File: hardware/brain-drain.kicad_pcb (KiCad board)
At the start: 4 copper layers, 150 x 112 mm, 302 parts, among them J10 SATA 22-pin, J11 SATA 22-pin, J12 SATA 22-pin, J13 SATA 22-pin, J21 KPJX-4S-S, J3 microSD, J40 Fan GND/5V/TACH/PWM, J41 OLED GND/VCC/SCL/SDA, J5 USB-C rpiboot, J50 M.2 M-key, J6 nRPIBOOT, J7 UART0 GND/TX/RX, M1 CM5002016, Q20 AO4407A, Q31 P-FET -30V 6A DFN3x3, Q32 P-FET -30V 6A DFN3x3, Q33 P-FET -30V 6A DFN3x3, Q34 P-FET -30V 6A DFN3x3, Q41 P-FET -30V 6A DFN3x3, Q42 P-FET -30V 6A DFN3x3, Q43 P-FET -30V 6A DFN3x3, Q44 P-FET -30V 6A DFN3x3, Q51 2N7002, Q52 2N7002, Q53 2N7002, Q54 2N7002, Q61 2N7002, Q62 2N7002, Q63 2N7002, Q64 2N7002, SW1 DIP x8, SW3 lid microswitch, U1 USB5744/2G, U10 ASM1153E, U11 ASM1153E, U12 ASM1153E, U13 ASM1153E, U2 USB5744/2G, U20 TPS56637RPAR, U21 TPS56637RPAR, U22 AP63203WU-7, U3 AP2112K-1.2, U50 TPS22965DSGR, U51 AP63203WU-7, U52 TPS22965DSGR, Y1 25MHz CL=20pF, Y10 30MHz CL=16pF, Y11 30MHz CL=16pF, Y12 30MHz CL=16pF, Y13 30MHz CL=16pF, Y2 25MHz CL=20pF

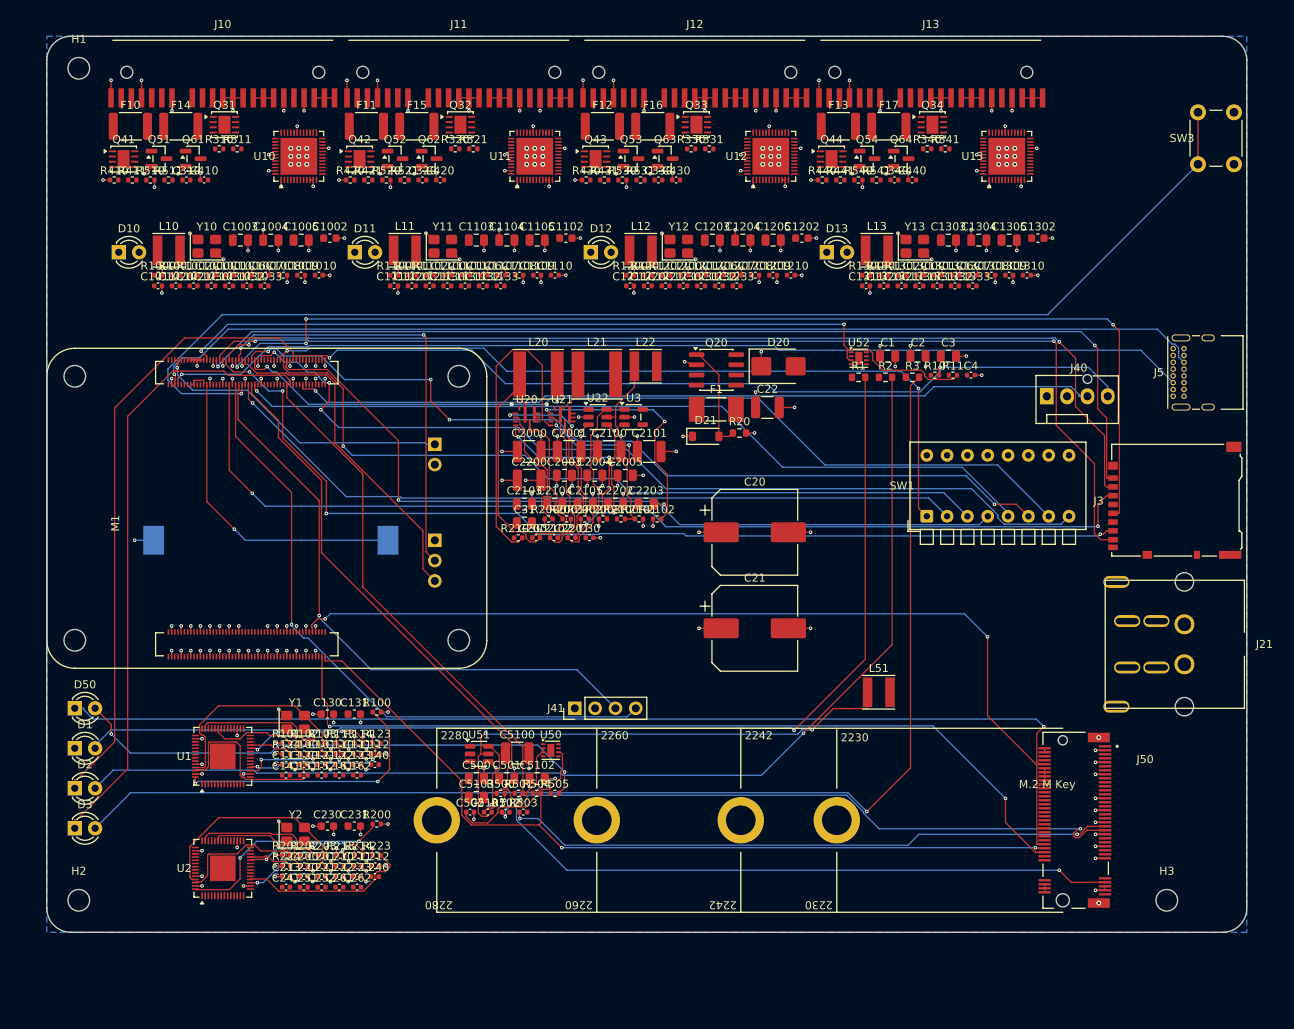
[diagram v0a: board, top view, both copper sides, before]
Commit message: hw(v3): staged autoroute on the 150x112 board — 83 % of connections, 21 of 48 pairs, DRC copper-clean
- stage 2 rerun after stripping the QFN via rings (the connector fanout now skips QFNs), stage 3 on
  freerouting 2.4.1, drc-clean, final fanouts: 3300 segments, 738 vias, 151 connections open
- docs: STATUS board row / R4 / R22, D7 outcome and D8 (0.3/0.15 mm vias for the QFN supply pins),
  CHANGELOG, tracker, README, FABRICATION gate 1; board renders

Co-Authored-By: Claude Fable 5.1 <noreply@anthropic.com>
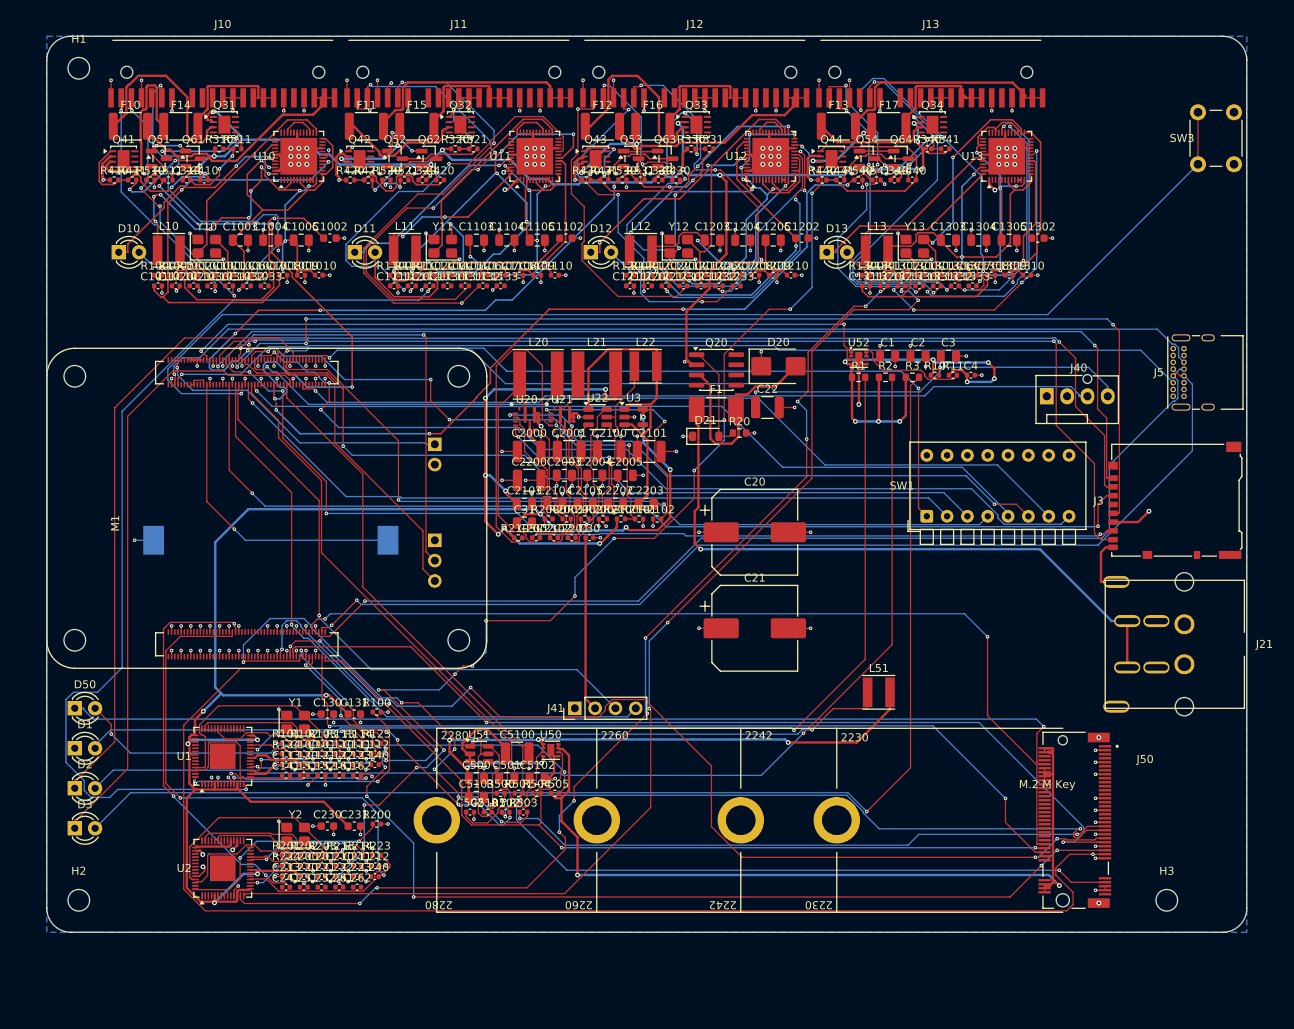
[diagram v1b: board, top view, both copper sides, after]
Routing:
- net +1V2: track 0.00 -> 213.0 mm, vias 0 -> 10
- net +12V: track 24.1 -> 198.6 mm, vias 14 -> 28
- net PCIE_CLK_P: track 0.00 -> 165.5 mm, vias 0 -> 1
- net BAY3_USB3_RX_N: track 0.00 -> 143.1 mm, vias 0 -> 16
- net BAY4_USB3_TX_N: track 0.00 -> 140.4 mm, vias 0 -> 4
- net BAY4_USB3_TX_P: track 0.00 -> 133.9 mm, vias 0 -> 10
- net USB2_DM: track 0.00 -> 130.5 mm, vias 0 -> 2
- net USB2_DP: track 0.00 -> 129.8 mm, vias 0 -> 1
- net PCIE_CLK_N: track 0.00 -> 128.3 mm, vias 0 -> 8
- net PCIE_TX_N: track 0.00 -> 124.1 mm, vias 0 -> 5
- net BAY2_USB3_TX_N: track 0.00 -> 120.3 mm, vias 0 -> 2
- net +3V3: track 24.9 -> 143.3 mm, vias 28 -> 30
- net PCIE_TX_P: track 0.00 -> 118.3 mm, vias 0 -> 2
- net 3V3_M2_SW: track 3.50 -> 106.5 mm, vias 0 -> 2
- net BAY_EN4: track 0.00 -> 95.6 mm, vias 0 -> 4
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
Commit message: hw(routing): D8 applied — 0.3/0.15 mm dog-bone vias on the QFN pins (fanout_qfn), unattended routing chain; D9 brief on bay cards / 8 ports
- route.py: fanout_qfn (two staggered via lines, all multi-pin non-pair nets), min via 0.3/0.15 and hole
  clearance 0.2 in the project rules; tools/route_chain.sh runs stage 2, stage 3, cleanup, fanouts,
  reports and renders unattended
- fresh v3 board with all four fanouts: 441 vias before routing, DRC clean; stage 1 routed in 2 minutes
- docs: decisions/2026-09-23-bay-cards.md (D9), DECISIONS D8/D9

Co-Authored-By: Claude Fable 5.1 <noreply@anthropic.com>
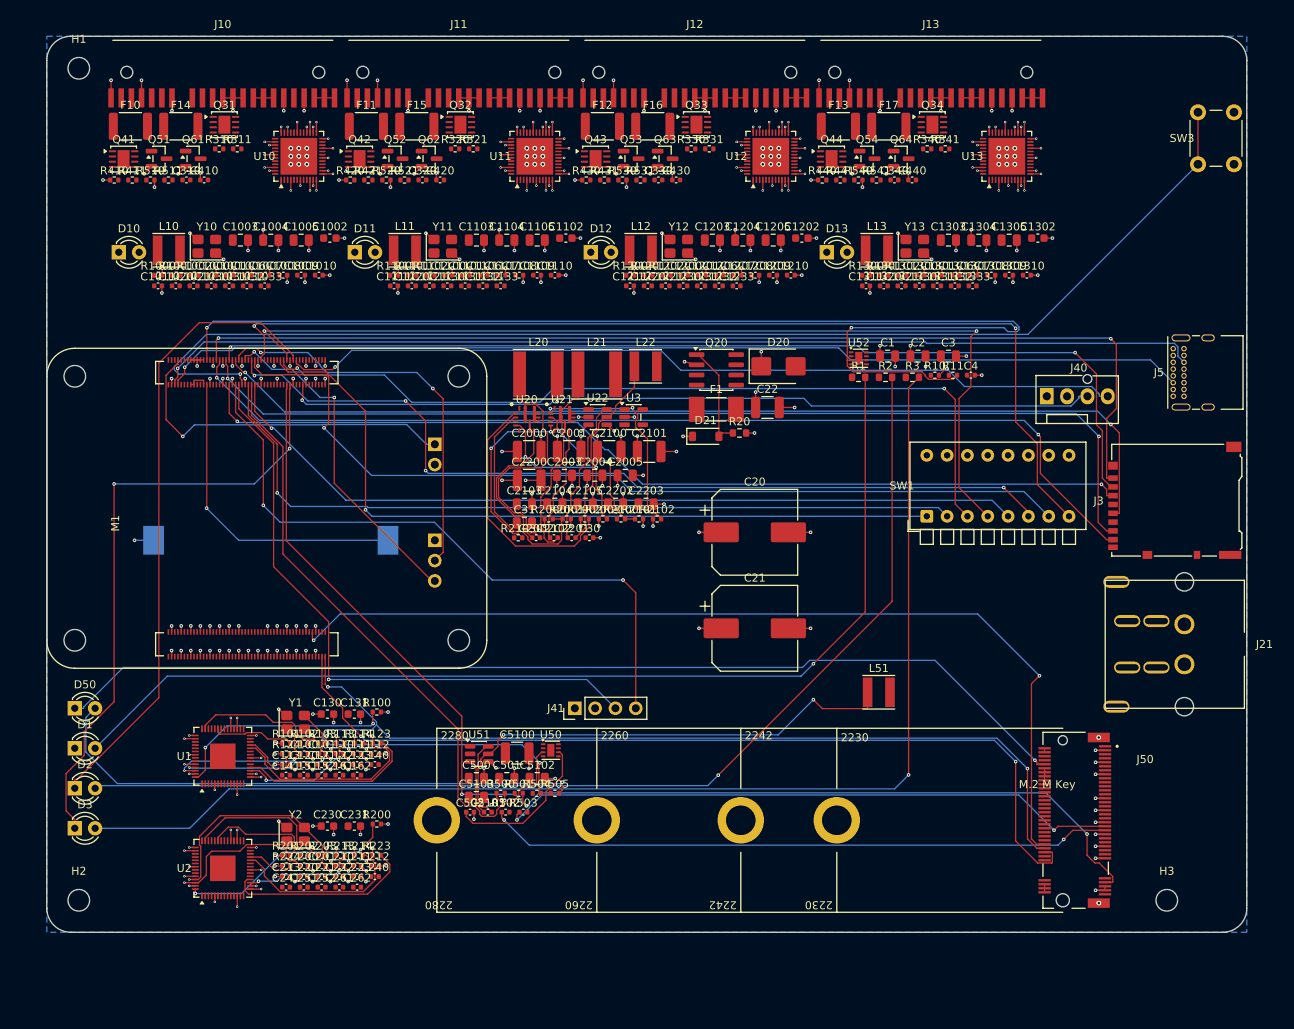
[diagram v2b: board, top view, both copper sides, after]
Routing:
- net +1V2: track 213.0 -> 17.0 mm, vias 10 -> 16
- net +12V: track 198.6 -> 24.1 mm, vias 28 -> 14
- net PCIE_CLK_P: track 165.5 -> 0.00 mm, vias 1 -> 0
- net BAY3_USB3_RX_N: track 143.1 -> 0.00 mm, vias 16 -> 0
- net BAY4_USB3_TX_N: track 140.4 -> 0.00 mm, vias 4 -> 0
- net BAY4_USB3_TX_P: track 133.9 -> 0.00 mm, vias 10 -> 0
- net USB2_DM: track 130.5 -> 0.00 mm, vias 2 -> 0
- net USB2_DP: track 129.8 -> 0.00 mm, vias 1 -> 0
- net PCIE_CLK_N: track 128.3 -> 0.00 mm, vias 8 -> 0
- net PCIE_TX_N: track 124.1 -> 0.00 mm, vias 5 -> 0
- net BAY2_USB3_TX_N: track 120.3 -> 0.00 mm, vias 2 -> 0
- net PCIE_TX_P: track 118.3 -> 0.00 mm, vias 2 -> 0
- net +3V3: track 143.3 -> 26.6 mm, vias 30 -> 28
- net 3V3_M2_SW: track 106.5 -> 3.50 mm, vias 2 -> 0
- net BAY_EN4: track 95.6 -> 0.00 mm, vias 4 -> 0
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
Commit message: docs: C24 brain + bay cards — decisions, architecture, BOM card table, fabrication, README, USAGE, STATUS, changelog, history; diagrams: 8 slots, lid plan, left wall
Co-Authored-By: Claude Fable 5.1 <noreply@anthropic.com>
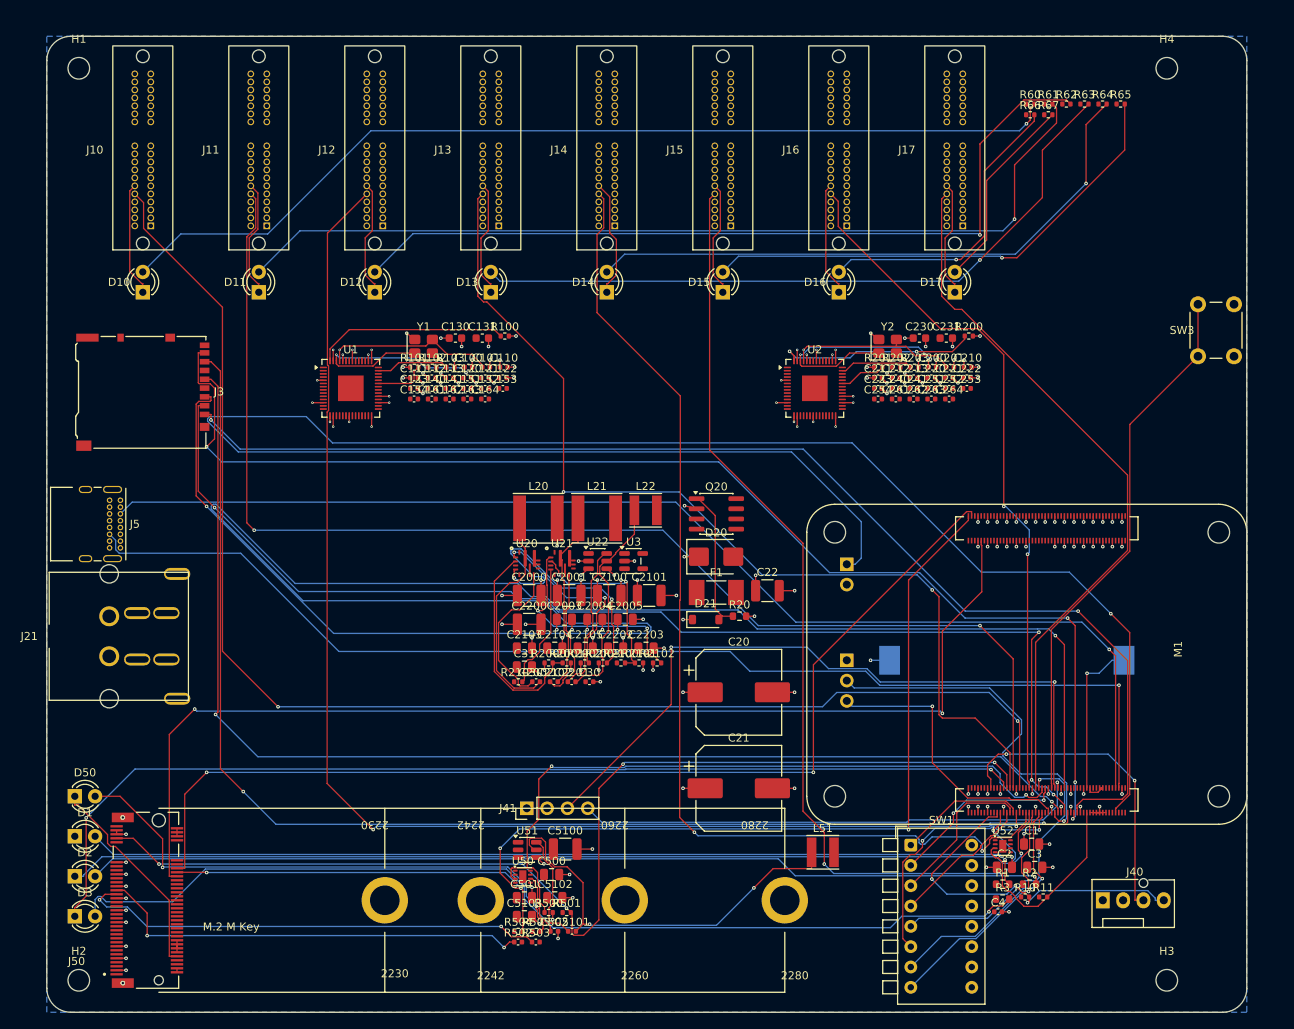
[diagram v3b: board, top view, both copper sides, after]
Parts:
- removed C1008, C1009, C1010, C1011, C1020, C1021, C1106, C1107, C1108, C1109, C1110, C1111, C1120, C1121, C1206, C1207, C1208, C1209, C1210, C1211, C1220, C1221, C1306, C1307, C1308, C1309, C1310, C1311, C1320, C1321, C310, C320, C330, C340, C410, C420, C430, C440: 100n, Capacitor_SMD:C_0402_1005Metric
- removed C1030, C1031, C1032, C1033, C1130, C1131, C1132, C1133, C1230, C1231, C1232, C1233, C1330, C1331, C1332, C1333: 10n, Capacitor_SMD:C_0402_1005Metric
- removed C1100, C1101, C1200, C1201, C1300, C1301: 22p, Capacitor_SMD:C_0402_1005Metric
- removed C1102, C1202, C1302: 2.2u, Capacitor_SMD:C_0603_1608Metric
- removed C1103, C1104, C1105, C1203, C1204, C1205, C1303, C1304, C1305: 10u 10V, Capacitor_SMD:C_0805_2012Metric
- removed F10, F11, F12, F13: 3A hold 1812, Fuse:Fuse_1812_4532Metric
- removed F14, F15, F16, F17: 2A hold 1812, Fuse:Fuse_1812_4532Metric
- removed L11, L12, L13: 4.7u 1A, Inductor_SMD:L_Taiyo-Yuden_NR-40xx
- removed Q31, Q32, Q33, Q34, Q41, Q42, Q43, Q44: P-FET -30V 6A DFN3x3, Package_DFN_QFN:DFN-8-1EP_3x3mm_P0.65mm_EP1.5x2.25mm
- removed Q51, Q52, Q53, Q54, Q61, Q62, Q63, Q64: 2N7002, Package_TO_SOT_SMD:SOT-23
- removed R1100, R1200, R1300: 12.1k 1%, Resistor_SMD:R_0402_1005Metric
- removed R1101, R1201, R1301, R311, R321, R331, R341, R411, R421, R431, R441, R510, R520, R530, R540: 10k, Resistor_SMD:R_0402_1005Metric
- removed R1102, R1202, R1302: 470, Resistor_SMD:R_0402_1005Metric
- removed R310, R320, R330, R340, R410, R420, R430, R440: 100k, Resistor_SMD:R_0402_1005Metric
- removed R511, R521, R531, R541: 1k, Resistor_SMD:R_0402_1005Metric
- removed Y11, Y12, Y13: 30MHz CL=16pF, Crystal:Crystal_SMD_3225-4Pin_3.2x2.5mm
- BT1: renamed from J6; value nRPIBOOT -> CR2032; footprint Connector_PinHeader_2.54mm:PinHeader_1x02_P2.54mm_Vertical -> Battery:BatteryHolder_Keystone_1060_1x2032
- C1: renamed from R3; value 1k -> 22u 10V; footprint Resistor_SMD:R_0603_1608Metric -> Capacitor_SMD:C_0805_2012Metric
- C101: renamed from C110; value 100n -> 33p
- C130: renamed from R103; value 200k -> 4.7u 10V; footprint Resistor_SMD:R_0402_1005Metric -> Capacitor_SMD:C_0603_1608Metric
- C131: renamed from R113; value 10k -> 4.7u 10V; footprint Resistor_SMD:R_0402_1005Metric -> Capacitor_SMD:C_0603_1608Metric
- C154: renamed from Y2; value 25MHz CL=20pF -> 100n; footprint Crystal:Crystal_SMD_3225-4Pin_3.2x2.5mm -> Capacitor_SMD:C_0402_1005Metric
- C161: renamed from C230; value 4.7u 10V -> 100n; footprint Capacitor_SMD:C_0603_1608Metric -> Capacitor_SMD:C_0402_1005Metric
- C162: renamed from C231; value 4.7u 10V -> 100n; footprint Capacitor_SMD:C_0603_1608Metric -> Capacitor_SMD:C_0402_1005Metric
- C163: renamed from R200; value 12.0k 1% -> 100n; footprint Resistor_SMD:R_0402_1005Metric -> Capacitor_SMD:C_0402_1005Metric
- C164: renamed from R201; value 10k -> 100n; footprint Resistor_SMD:R_0402_1005Metric -> Capacitor_SMD:C_0402_1005Metric
- C2: renamed from R10; value 10k -> 22u 10V; footprint Resistor_SMD:R_0402_1005Metric -> Capacitor_SMD:C_0805_2012Metric
- C2000: renamed from C2003; value 22u 10V -> 10u 25V; footprint Capacitor_SMD:C_0805_2012Metric -> Capacitor_SMD:C_1210_3225Metric
- C2001: renamed from C2004; value 22u 10V -> 10u 25V; footprint Capacitor_SMD:C_0805_2012Metric -> Capacitor_SMD:C_1210_3225Metric
- C2002: renamed from C5100; value 10u 25V -> 100n 25V; footprint Capacitor_SMD:C_1210_3225Metric -> Capacitor_SMD:C_0402_1005Metric
- C201: renamed from C210; value 100n -> 33p
- C21: renamed from L51; value 4.7u 3A -> 680u 25V low-ESR; footprint Inductor_SMD:L_Taiyo-Yuden_NR-40xx -> Capacitor_SMD:CP_Elec_10x10.5
- C2100: renamed from C2005; value 22u 10V -> 10u 25V; footprint Capacitor_SMD:C_0805_2012Metric -> Capacitor_SMD:C_1210_3225Metric
- C2101: renamed from C2103; value 22u 10V -> 10u 25V; footprint Capacitor_SMD:C_0805_2012Metric -> Capacitor_SMD:C_1210_3225Metric
- C2102: renamed from U50; value TPS22965DSGR -> 100n 25V; footprint Package_SON:Texas_DSG0008A_WSON-8-1EP_2x2mm_P0.5mm_EP0.9x1.6mm -> Capacitor_SMD:C_0402_1005Metric
- C2103: renamed from C31; value 10u 10V -> 22u 10V
- C2104: renamed from R2000; value 73.2k -> 22u 10V; footprint Resistor_SMD:R_0402_1005Metric -> Capacitor_SMD:C_0805_2012Metric
- C2105: renamed from R2001; value 10k -> 22u 10V; footprint Resistor_SMD:R_0402_1005Metric -> Capacitor_SMD:C_0805_2012Metric
- C22: renamed from L22; value 4.7u 3A -> 10u 25V; footprint Inductor_SMD:L_Taiyo-Yuden_NR-40xx -> Capacitor_SMD:C_1210_3225Metric
- C2200: renamed from C2104; value 22u 10V -> 10u 25V; footprint Capacitor_SMD:C_0805_2012Metric -> Capacitor_SMD:C_1210_3225Metric
- C2201: renamed from C500; value 10u 10V -> 100n 10V; footprint Capacitor_SMD:C_0805_2012Metric -> Capacitor_SMD:C_0402_1005Metric
- C2202: renamed from R2002; value 100k -> 22u 10V; footprint Resistor_SMD:R_0402_1005Metric -> Capacitor_SMD:C_0805_2012Metric
- C2203: renamed from R2003; value 10k -> 22u 10V; footprint Resistor_SMD:R_0402_1005Metric -> Capacitor_SMD:C_0805_2012Metric
- C230: renamed from R203; value 200k -> 4.7u 10V; footprint Resistor_SMD:R_0402_1005Metric -> Capacitor_SMD:C_0603_1608Metric
- C231: renamed from R213; value 10k -> 4.7u 10V; footprint Resistor_SMD:R_0402_1005Metric -> Capacitor_SMD:C_0603_1608Metric
- C254: renamed from L10; value 4.7u 1A -> 100n; footprint Inductor_SMD:L_Taiyo-Yuden_NR-40xx -> Capacitor_SMD:C_0402_1005Metric
- C261: renamed from Y10; value 30MHz CL=16pF -> 100n; footprint Crystal:Crystal_SMD_3225-4Pin_3.2x2.5mm -> Capacitor_SMD:C_0402_1005Metric
- C262: renamed from C1003; value 10u 10V -> 100n; footprint Capacitor_SMD:C_0805_2012Metric -> Capacitor_SMD:C_0402_1005Metric
- C263: renamed from C1004; value 10u 10V -> 100n; footprint Capacitor_SMD:C_0805_2012Metric -> Capacitor_SMD:C_0402_1005Metric
- C264: renamed from C1005; value 10u 10V -> 100n; footprint Capacitor_SMD:C_0805_2012Metric -> Capacitor_SMD:C_0402_1005Metric
- C3: renamed from R11; value 10k -> 10u 10V; footprint Resistor_SMD:R_0402_1005Metric -> Capacitor_SMD:C_0805_2012Metric
- C30: renamed from C501; value 22u 10V -> 1u 10V; footprint Capacitor_SMD:C_0805_2012Metric -> Capacitor_SMD:C_0402_1005Metric
- C31: renamed from R2100; value 73.2k -> 10u 10V; footprint Resistor_SMD:R_0402_1005Metric -> Capacitor_SMD:C_0805_2012Metric
- C4: renamed from R101; value 10k -> 1u 10V; footprint Resistor_SMD:R_0402_1005Metric -> Capacitor_SMD:C_0402_1005Metric
- C500: renamed from R501; value 10k -> 10u 10V; footprint Resistor_SMD:R_0402_1005Metric -> Capacitor_SMD:C_0805_2012Metric
- C501: renamed from R504; value 10k -> 22u 10V; footprint Resistor_SMD:R_0402_1005Metric -> Capacitor_SMD:C_0805_2012Metric
- C502: renamed from C1; value 22u 10V -> 1n; footprint Capacitor_SMD:C_0805_2012Metric -> Capacitor_SMD:C_0402_1005Metric
- C5100: renamed from C5103; value 22u 10V -> 10u 25V; footprint Capacitor_SMD:C_0805_2012Metric -> Capacitor_SMD:C_1210_3225Metric
- C5101: renamed from C2; value 22u 10V -> 100n 10V; footprint Capacitor_SMD:C_0805_2012Metric -> Capacitor_SMD:C_0402_1005Metric
- C5102: renamed from R505; value 470 -> 22u 10V; footprint Resistor_SMD:R_0402_1005Metric -> Capacitor_SMD:C_0805_2012Metric
- C5103: renamed from C502; value 1n -> 22u 10V; footprint Capacitor_SMD:C_0402_1005Metric -> Capacitor_SMD:C_0805_2012Metric
- D1: renamed from D2; value green ACT -> green PWR
- D10: value blue bay activity -> blue bay 1 activity
- D11: renamed from J11; value SATA 22-pin -> blue bay 2 activity; footprint brain-drain:SATA_22pin_Receptacle_RA -> LED_THT:LED_D3.0mm
- D12: renamed from U12; value ASM1153E -> blue bay 3 activity; footprint Package_DFN_QFN:QFN-48-1EP_6x6mm_P0.4mm_EP4.6x4.6mm -> LED_THT:LED_D3.0mm
- D13: renamed from D12; value blue bay activity -> blue bay 4 activity
- D14: renamed from J13; value SATA 22-pin -> blue bay 5 activity; footprint brain-drain:SATA_22pin_Receptacle_RA -> LED_THT:LED_D3.0mm
- D15: renamed from J50; value M.2 M-key -> blue bay 6 activity; footprint brain-drain:M2_Socket3_MKey_CM5IO -> LED_THT:LED_D3.0mm
- D16: renamed from SW3; value lid microswitch -> blue bay 7 activity; footprint Button_Switch_THT:SW_PUSH_6mm -> LED_THT:LED_D3.0mm
- D17: renamed from D20; value SMBJ15A -> blue bay 8 activity; footprint Diode_SMD:D_SMB -> LED_THT:LED_D3.0mm
- D2: renamed from D3; value red STATUS -> green ACT
- D20: renamed from L20; value 2.2u 8A -> SMBJ15A; footprint Inductor_SMD:L_Taiyo-Yuden_NR-60xx -> Diode_SMD:D_SMB
- D21: renamed from U20; value TPS56637RPAR -> 12V 0.5W; footprint brain-drain:Texas_RPA0010A_VQFN-HR-10_3x3mm -> Diode_SMD:D_SOD-123
- D3: renamed from SW1; value DIP x8 -> red STATUS; footprint Button_Switch_THT:SW_DIP_SPSTx08_Piano_10.8x21.88mm_W7.62mm_P2.54mm -> LED_THT:LED_D3.0mm
- D50: renamed from C22; value 10u 25V -> blue M.2 activity; footprint Capacitor_SMD:C_1210_3225Metric -> LED_THT:LED_D3.0mm
- F1: renamed from L21; value 2.2u 8A -> 10A slow 0453010.MR; footprint Inductor_SMD:L_Taiyo-Yuden_NR-60xx -> Fuse:Fuse_Littelfuse-NANO2-451_453
- H4: renamed from J21; value KPJX-4S-S -> M2.5; footprint brain-drain:Kycon_KPJX-4S-S -> MountingHole:MountingHole_2.7mm_M2.5
- J10: value SATA 22-pin -> bay slot 1; footprint brain-drain:SATA_22pin_Receptacle_RA -> brain-drain:PCIe_x1_Socket_THT
- J11: renamed from U11; value ASM1153E -> bay slot 2; footprint Package_DFN_QFN:QFN-48-1EP_6x6mm_P0.4mm_EP4.6x4.6mm -> brain-drain:PCIe_x1_Socket_THT
- J12: renamed from D11; value blue bay activity -> bay slot 3; footprint LED_THT:LED_D3.0mm -> brain-drain:PCIe_x1_Socket_THT
- J13: renamed from J12; value SATA 22-pin -> bay slot 4; footprint brain-drain:SATA_22pin_Receptacle_RA -> brain-drain:PCIe_x1_Socket_THT
- J14: renamed from U13; value ASM1153E -> bay slot 5; footprint Package_DFN_QFN:QFN-48-1EP_6x6mm_P0.4mm_EP4.6x4.6mm -> brain-drain:PCIe_x1_Socket_THT
- J15: renamed from D13; value blue bay activity -> bay slot 6; footprint LED_THT:LED_D3.0mm -> brain-drain:PCIe_x1_Socket_THT
- J16: renamed from D50; value blue M.2 activity -> bay slot 7; footprint LED_THT:LED_D3.0mm -> brain-drain:PCIe_x1_Socket_THT
- J17: renamed from Q20; value AO4407A -> bay slot 8; footprint Package_SO:SOIC-8_3.9x4.9mm_P1.27mm -> brain-drain:PCIe_x1_Socket_THT
- J21: renamed from C20; value 680u 25V low-ESR -> KPJX-4S-S; footprint Capacitor_SMD:CP_Elec_10x10.5 -> brain-drain:Kycon_KPJX-4S-S
- J3: renamed from J5; value USB-C rpiboot -> microSD; footprint Connector_USB:USB_C_Receptacle_GCT_USB4085 -> Connector_Card:microSD_HC_Hirose_DM3AT-SF-PEJM5
- J40: renamed from D1; value green PWR -> Fan GND/5V/TACH/PWM; footprint LED_THT:LED_D3.0mm -> Connector:FanPinHeader_1x04_P2.54mm_Vertical
- J41: renamed from J3; value microSD -> OLED GND/VCC/SCL/SDA; footprint Connector_Card:microSD_HC_Hirose_DM3AT-SF-PEJM5 -> Connector_PinHeader_2.54mm:PinHeader_1x04_P2.54mm_Vertical
- J5: renamed from U1; value USB5744/2G -> USB-C rpiboot; footprint Package_DFN_QFN:QFN-56-1EP_7x7mm_P0.4mm_EP3.2x3.2mm -> Connector_USB:USB_C_Receptacle_GCT_USB4085
- J50: renamed from F1; value 10A slow 0453010.MR -> M.2 M-key; footprint Fuse:Fuse_Littelfuse-NANO2-451_453 -> brain-drain:M2_Socket3_MKey_CM5IO
- J6: renamed from J7; value UART0 GND/TX/RX -> nRPIBOOT; footprint Connector_PinHeader_2.54mm:PinHeader_1x03_P2.54mm_Vertical -> Connector_PinHeader_2.54mm:PinHeader_1x02_P2.54mm_Vertical
- J7: renamed from J40; value Fan GND/5V/TACH/PWM -> UART0 GND/TX/RX; footprint Connector:FanPinHeader_1x04_P2.54mm_Vertical -> Connector_PinHeader_2.54mm:PinHeader_1x03_P2.54mm_Vertical; moved to B.Cu
- L20: renamed from U22; value AP63203WU-7 -> 2.2u 8A; footprint Package_TO_SOT_SMD:TSOT-23-6 -> Inductor_SMD:L_Taiyo-Yuden_NR-60xx
- L21: renamed from U3; value AP2112K-1.2 -> 2.2u 8A; footprint Package_TO_SOT_SMD:SOT-23-5 -> Inductor_SMD:L_Taiyo-Yuden_NR-60xx
- L22: renamed from C2000; value 10u 25V -> 4.7u 3A; footprint Capacitor_SMD:C_1210_3225Metric -> Inductor_SMD:L_Taiyo-Yuden_NR-40xx
- L51: renamed from M1; value CM5002016 -> 4.7u 3A; footprint brain-drain:Raspberry-Pi-5-Compute-Module -> Inductor_SMD:L_Taiyo-Yuden_NR-40xx
- M1: renamed from BT1; value CR2032 -> CM5002016; footprint Battery:BatteryHolder_Keystone_1060_1x2032 -> brain-drain:Raspberry-Pi-5-Compute-Module; moved to F.Cu
- Q20: renamed from R20; value 100k -> AO4407A; footprint Resistor_SMD:R_0603_1608Metric -> Package_SO:SOIC-8_3.9x4.9mm_P1.27mm
- R1: renamed from C4; value 1u 10V -> 1k; footprint Capacitor_SMD:C_0402_1005Metric -> Resistor_SMD:R_0603_1608Metric
- R10: renamed from C131; value 4.7u 10V -> 10k; footprint Capacitor_SMD:C_0603_1608Metric -> Resistor_SMD:R_0402_1005Metric
- R100: renamed from R114; value 10k -> 12.0k 1%
- R103: renamed from C100; value 33p -> 200k; footprint Capacitor_SMD:C_0402_1005Metric -> Resistor_SMD:R_0402_1005Metric
- R11: renamed from R100; value 12.0k 1% -> 10k
- R2: renamed from Y1; value 25MHz CL=20pF -> 1k; footprint Crystal:Crystal_SMD_3225-4Pin_3.2x2.5mm -> Resistor_SMD:R_0603_1608Metric
- R20: renamed from U21; value TPS56637RPAR -> 100k; footprint brain-drain:Texas_RPA0010A_VQFN-HR-10_3x3mm -> Resistor_SMD:R_0603_1608Metric
- R200: renamed from R214; value 10k -> 12.0k 1%
- R2000: renamed from R2101; value 10k -> 73.2k
- R2001: renamed from R2102; value 100k -> 10k
- R2002: renamed from R2103; value 10k -> 100k
- R2003: renamed from C2002; value 100n 25V -> 10k; footprint Capacitor_SMD:C_0402_1005Metric -> Resistor_SMD:R_0402_1005Metric
- R203: renamed from C200; value 33p -> 200k; footprint Capacitor_SMD:C_0402_1005Metric -> Resistor_SMD:R_0402_1005Metric
- R2100: renamed from C2102; value 100n 25V -> 73.2k; footprint Capacitor_SMD:C_0402_1005Metric -> Resistor_SMD:R_0402_1005Metric
- R2101: renamed from C2201; value 100n 10V -> 10k; footprint Capacitor_SMD:C_0402_1005Metric -> Resistor_SMD:R_0402_1005Metric
- R2102: renamed from C30; value 1u 10V -> 100k; footprint Capacitor_SMD:C_0402_1005Metric -> Resistor_SMD:R_0402_1005Metric
- R2103: renamed from U51; value AP63203WU-7 -> 10k; footprint Package_TO_SOT_SMD:TSOT-23-6 -> Resistor_SMD:R_0402_1005Metric
- R3: renamed from C130; value 4.7u 10V -> 1k; footprint Capacitor_SMD:C_0603_1608Metric -> Resistor_SMD:R_0603_1608Metric
- R500: renamed from C5101; value 100n 10V -> 10k; footprint Capacitor_SMD:C_0402_1005Metric -> Resistor_SMD:R_0402_1005Metric
- R501: renamed from R502; value 0R (cap DNP alt) -> 10k; footprint Capacitor_SMD:C_0402_1005Metric -> Resistor_SMD:R_0402_1005Metric
- R502: renamed from C3; value 10u 10V -> 0R (cap DNP alt); footprint Capacitor_SMD:C_0805_2012Metric -> Capacitor_SMD:C_0402_1005Metric
- R503: renamed from R1; value 1k -> 0R (cap DNP alt); footprint Resistor_SMD:R_0603_1608Metric -> Capacitor_SMD:C_0402_1005Metric
- R504: renamed from R503; value 0R (cap DNP alt) -> 10k; footprint Capacitor_SMD:C_0402_1005Metric -> Resistor_SMD:R_0402_1005Metric
- R505: renamed from U52; value TPS22965DSGR -> 470; footprint Package_SON:Texas_DSG0008A_WSON-8-1EP_2x2mm_P0.5mm_EP0.9x1.6mm -> Resistor_SMD:R_0402_1005Metric
- R60: renamed from C1002; value 2.2u -> 470; footprint Capacitor_SMD:C_0603_1608Metric -> Resistor_SMD:R_0402_1005Metric
- R61: renamed from R1000; value 12.1k 1% -> 470
- R62: renamed from R1001; value 10k -> 470
- R64: renamed from C1000; value 22p -> 470; footprint Capacitor_SMD:C_0402_1005Metric -> Resistor_SMD:R_0402_1005Metric
- R65: renamed from C1001; value 22p -> 470; footprint Capacitor_SMD:C_0402_1005Metric -> Resistor_SMD:R_0402_1005Metric
- R66: renamed from C1006; value 100n -> 470; footprint Capacitor_SMD:C_0402_1005Metric -> Resistor_SMD:R_0402_1005Metric
- R67: renamed from C1007; value 100n -> 470; footprint Capacitor_SMD:C_0402_1005Metric -> Resistor_SMD:R_0402_1005Metric
- SW1: renamed from J41; value OLED GND/VCC/SCL/SDA -> DIP x8; footprint Connector_PinHeader_2.54mm:PinHeader_1x04_P2.54mm_Vertical -> Button_Switch_THT:SW_DIP_SPSTx08_Piano_10.8x21.88mm_W7.62mm_P2.54mm
- SW3: renamed from D21; value 12V 0.5W -> lid microswitch; footprint Diode_SMD:D_SOD-123 -> Button_Switch_THT:SW_PUSH_6mm
- U2: renamed from U10; value ASM1153E -> USB5744/2G; footprint Package_DFN_QFN:QFN-48-1EP_6x6mm_P0.4mm_EP4.6x4.6mm -> Package_DFN_QFN:QFN-56-1EP_7x7mm_P0.4mm_EP3.2x3.2mm
- U20: renamed from C2001; value 10u 25V -> TPS56637RPAR; footprint Capacitor_SMD:C_1210_3225Metric -> brain-drain:Texas_RPA0010A_VQFN-HR-10_3x3mm
- U21: renamed from C2100; value 10u 25V -> TPS56637RPAR; footprint Capacitor_SMD:C_1210_3225Metric -> brain-drain:Texas_RPA0010A_VQFN-HR-10_3x3mm
- U22: renamed from C2101; value 10u 25V -> AP63203WU-7; footprint Capacitor_SMD:C_1210_3225Metric -> Package_TO_SOT_SMD:TSOT-23-6
- U3: renamed from C2200; value 10u 25V -> AP2112K-1.2; footprint Capacitor_SMD:C_1210_3225Metric -> Package_TO_SOT_SMD:SOT-23-5
- U50: renamed from R500; value 10k -> TPS22965DSGR; footprint Resistor_SMD:R_0402_1005Metric -> Package_SON:Texas_DSG0008A_WSON-8-1EP_2x2mm_P0.5mm_EP0.9x1.6mm
- U51: renamed from C5102; value 22u 10V -> AP63203WU-7; footprint Capacitor_SMD:C_0805_2012Metric -> Package_TO_SOT_SMD:TSOT-23-6
- U52: renamed from R2; value 1k -> TPS22965DSGR; footprint Resistor_SMD:R_0603_1608Metric -> Package_SON:Texas_DSG0008A_WSON-8-1EP_2x2mm_P0.5mm_EP0.9x1.6mm
- Y1: renamed from R102; value 10k -> 25MHz CL=20pF; footprint Resistor_SMD:R_0402_1005Metric -> Crystal:Crystal_SMD_3225-4Pin_3.2x2.5mm
- Y2: renamed from R202; value 10k -> 25MHz CL=20pF; footprint Resistor_SMD:R_0402_1005Metric -> Crystal:Crystal_SMD_3225-4Pin_3.2x2.5mm
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- renumbered C101 to C100, C111 to C110, C112 to C111, C113 to C112, C120 to C113, C121 to C120, C122 to C121, C123 to C122, C140 to C123, C141 to C140, C151 to C141, C152 to C151, C161 to C152, C162 to C153, C21 to C20, C201 to C200, C2105 to C2003, C2202 to C2004, C2203 to C2005, C211 to C210, C212 to C211, C213 to C212, C220 to C213, C221 to C220, C222 to C221, C223 to C222, C240 to C223, C241 to C240, C251 to C241, C252 to C251, C261 to C252, C262 to C253, R123 to R101, R124 to R102, R223 to R201, R224 to R202, R1002 to R63, U2 to U1
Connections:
- BT1 pad 1: nRPIBOOT -> VBAT
- C1 pad 1: +3V3 -> 5V_SYS
- C1 pad 2: D3_A -> GND
- C100 pad 1: U1_XTALO -> U1_XTALI
- C101 pad 1: +3V3 -> U1_XTALO
- C113 pad 1: +1V2 -> +3V3
- C123 pad 1: U1_UP_TXDP -> +1V2
- C123 pad 2: USB3_0_RX_P -> GND
- C130 pad 1: U1_CFG_NON_REM -> +3V3
- C131 pad 1: +3V3 -> +1V2
- C131 pad 2: U1_PRT_DIS_P3 -> GND
- C140 pad 1: U1_UP_TXDM -> U1_UP_TXDP
- C140 pad 2: USB3_0_RX_N -> USB3_0_RX_P
- C141 pad 1: U1_DN1_TXDP -> U1_UP_TXDM
- C141 pad 2: BAY1_USB3_RX_P -> USB3_0_RX_N
- C151 pad 1: U1_DN2_TXDP -> U1_DN1_TXDP
- C151 pad 2: BAY2_USB3_RX_P -> BAY1_USB3_RX_P
- C152 pad 1: U1_DN1_TXDM -> U1_DN2_TXDP
- C152 pad 2: BAY1_USB3_RX_N -> BAY2_USB3_RX_P
- C153 pad 1: U1_DN2_TXDM -> U1_DN3_TXDP
- C153 pad 2: BAY2_USB3_RX_N -> BAY3_USB3_RX_P
- C154 pad 1: U2_XTALI -> U1_DN4_TXDP
- C154 pad 2: GND -> BAY4_USB3_RX_P
- C161 pad 1: +3V3 -> U1_DN1_TXDM
- C161 pad 2: GND -> BAY1_USB3_RX_N
- C162 pad 1: +1V2 -> U1_DN2_TXDM
- C162 pad 2: GND -> BAY2_USB3_RX_N
- C163 pad 1: U2_RBIAS -> U1_DN3_TXDM
- C163 pad 2: GND -> BAY3_USB3_RX_N
- C164 pad 1: +3V3 -> U1_DN4_TXDM
- C164 pad 2: U2_VBUS_DET -> BAY4_USB3_RX_N
- C2 pad 1: +3V3 -> 5V_SYS
- C2 pad 2: FAN_PWM -> GND
- C200 pad 1: U2_XTALO -> U2_XTALI
- C2000 pad 1: 5V_SYS -> +12V
- C2001 pad 1: 5V_SYS -> +12V
- C2002 pad 1: +12V -> U20_BOOT
- C2002 pad 2: GND -> U20_SW
- C2003 pad 1: 5V_HDD -> 5V_SYS
- C2004 pad 1: +3V3 -> 5V_SYS
- C2005 pad 1: +3V3 -> 5V_SYS
- C201 pad 1: +3V3 -> U2_XTALO
- C21 pad 1: U51_SW -> +12V
- C21 pad 2: 3V3_M2 -> GND
- C2100 pad 1: 5V_SYS -> +12V
- C2101 pad 1: 5V_HDD -> +12V
- C2102 pad 1: 3V3_M2 -> U21_BOOT
- C2102 pad 2: 3V3_M2 -> U21_SW
- C2103 pad 1: +1V2 -> 5V_HDD
- C2104 pad 1: 5V_SYS -> 5V_HDD
- C2104 pad 2: U20_FB -> GND
- C2105 pad 1: U20_FB -> 5V_HDD
- C213 pad 1: +1V2 -> +3V3
- C22 pad 1: U22_SW -> +12V
- C22 pad 2: +3V3 -> GND
- C2200 pad 1: 5V_HDD -> +12V
- C2201 pad 1: 3V3_M2 -> U22_BST
- C2201 pad 2: GND -> U22_SW
- C2202 pad 1: +12V -> +3V3
- C2202 pad 2: U20_EN -> GND
- C2203 pad 1: 5V_SYS -> +3V3
- C2203 pad 2: PG_5V_SYS -> GND
- C223 pad 1: U2_UP_TXDP -> +1V2
- C223 pad 2: USB3_1_RX_P -> GND
- C230 pad 1: U2_CFG_NON_REM -> +3V3
- C231 pad 1: +3V3 -> +1V2
- C231 pad 2: U2_PRT_DIS_P3 -> GND
- C240 pad 1: U2_UP_TXDM -> U2_UP_TXDP
- C240 pad 2: USB3_1_RX_N -> USB3_1_RX_P
- C241 pad 1: U2_DN1_TXDP -> U2_UP_TXDM
- C241 pad 2: BAY3_USB3_RX_P -> USB3_1_RX_N
- C251 pad 1: U2_DN2_TXDP -> U2_DN1_TXDP
- C251 pad 2: BAY4_USB3_RX_P -> BAY5_USB3_RX_P
- C252 pad 1: U2_DN1_TXDM -> U2_DN2_TXDP
- C252 pad 2: BAY3_USB3_RX_N -> BAY6_USB3_RX_P
- C253 pad 1: U2_DN2_TXDM -> U2_DN3_TXDP
- C253 pad 2: BAY4_USB3_RX_N -> BAY7_USB3_RX_P
- C254 pad 1: U10_LXI -> U2_DN4_TXDP
- C254 pad 2: U10_VDD_CORE -> BAY8_USB3_RX_P
- C261 pad 1: U10_XI -> U2_DN1_TXDM
- C261 pad 2: GND -> BAY5_USB3_RX_N
- C262 pad 1: U10_VDD_CORE -> U2_DN2_TXDM
- C262 pad 2: GND -> BAY6_USB3_RX_N
- C263 pad 1: 5V_SYS -> U2_DN3_TXDM
- C263 pad 2: GND -> BAY7_USB3_RX_N
- C264 pad 1: U10_VCCO -> U2_DN4_TXDM
- C264 pad 2: GND -> BAY8_USB3_RX_N
- C3 pad 1: +3V3 -> SD_VDD
- C3 pad 2: SD_PWR_ON -> GND
- C30 pad 1: 3V3_M2_SW -> +3V3
- C31 pad 1: 5V_HDD -> +1V2
- C31 pad 2: U21_FB -> GND
- C4 pad 2: U1_VBUS_DET -> GND
- C500 pad 1: 3V3_M2_SW -> 3V3_M2
- C500 pad 2: M2_PEDET -> GND
- C501 pad 2: PCIE_CLKREQ -> GND
- C502 pad 1: 5V_SYS -> U50_CT
- C5100 pad 1: 3V3_M2 -> +12V
- C5101 pad 1: 5V_SYS -> U51_BST
- C5101 pad 2: GND -> U51_SW
- C5102 pad 1: 3V3_M2_SW -> 3V3_M2
- C5102 pad 2: M2_LED_A -> GND
- C5103 pad 1: U50_CT -> 3V3_M2
- D1 pad 1: LED_nACT -> GND
- D1 pad 2: D2_A -> D1_A
- D10 pad 1: U10_LED -> BAY1_LED_K
- D12 pad 1: 5V_SYS -> BAY3_LED_K
- D12 pad 2: (no net) -> BAY3_LED_A
- D13 pad 1: U12_LED -> BAY4_LED_K
- D13 pad 2: BAY3_LED_A -> BAY4_LED_A
- D15 pad 1: (no net) -> BAY6_LED_K
- D15 pad 2: 3V3_M2_SW -> BAY6_LED_A
- D16 pad 1: M2_DOOR -> BAY7_LED_K
- D16 pad 2: GND -> BAY7_LED_A
- D17 pad 1: GND -> BAY8_LED_K
- D17 pad 2: VIN_12V_FUSED -> BAY8_LED_A
- D2 pad 1: STATUS_LED -> LED_nACT
- D2 pad 2: D3_A -> D2_A
- D20 pad 1: U20_SW -> GND
- D20 pad 2: 5V_SYS -> VIN_12V_FUSED
- D21 pad 1: U20_EN -> +12V
- D21 pad 2: U20_FB -> Q20_GATE
- D3 pad 1: DIP1 -> STATUS_LED
- D3 pad 2: DIP2 -> D3_A
- D50 pad 1: +12V -> M2_DAS
- D50 pad 2: GND -> M2_LED_A
- F1 pad 1: U21_SW -> VIN_12V_RAW
- F1 pad 2: 5V_HDD -> VIN_12V_FUSED
- J21 pad 1: +12V -> VIN_12V_RAW
- J21 pad 2: GND -> VIN_12V_RAW
- J40 pad 2: D1_A -> 5V_SYS
- J41 pad 1: SD_DAT2 -> GND
- J41 pad 2: SD_DAT3 -> +3V3
- J41 pad 3: SD_CMD -> I2C1_SCL
- J41 pad 4: SD_VDD -> I2C1_SDA
- J50 pad 1: VIN_12V_RAW -> (no net)
- J50 pad 2: VIN_12V_FUSED -> 3V3_M2_SW
- J6 pad 1: GND -> nRPIBOOT
- J6 pad 2: UART0_TXD -> GND
- J7 pad 2: 5V_SYS -> UART0_TXD
- J7 pad 3: FAN_TACHO -> UART0_RXD
- L20 pad 1: +3V3 -> U20_SW
- L20 pad 2: +12V -> 5V_SYS
- L21 pad 1: +3V3 -> U21_SW
- L21 pad 2: GND -> 5V_HDD
- L22 pad 1: +12V -> U22_SW
- L22 pad 2: GND -> +3V3
- L51 pad 1: GND -> U51_SW
- L51 pad 2: GND -> 3V3_M2
- M1 pad 1: VBAT -> GND
- Q20 pad 2: GND -> +12V
- R1 pad 2: GND -> D1_A
- R10 pad 1: +1V2 -> +3V3
- R10 pad 2: GND -> FAN_PWM
- R100 pad 1: +3V3 -> U1_RBIAS
- R100 pad 2: U1_PRT_DIS_P4 -> GND
- R101 pad 2: U1_PRT_DIS_M3 -> U1_VBUS_DET
- R102 pad 2: U1_PRT_DIS_M4 -> U1_RESET_N
- R103 pad 1: U1_XTALI -> U1_CFG_NON_REM
- R11 pad 1: U1_RBIAS -> +3V3
- R11 pad 2: GND -> SD_PWR_ON
- R2 pad 1: U1_XTALI -> +3V3
- R2 pad 2: GND -> D2_A
- R20 pad 1: U21_EN -> Q20_GATE
- R20 pad 2: U21_FB -> GND
- R200 pad 1: +3V3 -> U2_RBIAS
- R200 pad 2: U2_PRT_DIS_P4 -> GND
- R2000 pad 1: U21_FB -> 5V_SYS
- R2000 pad 2: GND -> U20_FB
- R2001 pad 1: +12V -> U20_FB
- R2001 pad 2: U21_EN -> GND
- R2002 pad 1: 5V_HDD -> +12V
- R2002 pad 2: PG_5V_HDD -> U20_EN
- R2003 pad 1: U20_BOOT -> 5V_SYS
- R2003 pad 2: U20_SW -> PG_5V_SYS
- R201 pad 2: U2_PRT_DIS_M3 -> U2_VBUS_DET
- R202 pad 2: U2_PRT_DIS_M4 -> U2_RESET_N
- R203 pad 1: U2_XTALI -> U2_CFG_NON_REM
- R2100 pad 1: U21_BOOT -> 5V_HDD
- R2100 pad 2: U21_SW -> U21_FB
- R2101 pad 1: U22_BST -> U21_FB
- R2101 pad 2: U22_SW -> GND
- R2102 pad 1: +3V3 -> +12V
- R2102 pad 2: GND -> U21_EN
- R2103 pad 1: 3V3_M2 -> 5V_HDD
- R2103 pad 2: +12V -> PG_5V_HDD
- R3 pad 2: GND -> D3_A
- R500 pad 1: U51_BST -> M2_PWR_EN
- R500 pad 2: U51_SW -> GND
- R501 pad 1: M2_PERp0 -> 3V3_M2_SW
- R501 pad 2: PCIE_RX_P -> M2_PEDET
- R502 pad 1: SD_VDD -> M2_PERp0
- R502 pad 2: GND -> PCIE_RX_P
- R503 pad 1: +3V3 -> M2_PERn0
- R503 pad 2: D1_A -> PCIE_RX_N
- R504 pad 1: M2_PERn0 -> 3V3_M2_SW
- R504 pad 2: PCIE_RX_N -> PCIE_CLKREQ
- R505 pad 1: +3V3 -> 3V3_M2_SW
- R505 pad 2: +3V3 -> M2_LED_A
- R60 pad 1: U10_RST -> +3V3
- R60 pad 2: GND -> BAY1_LED_A
- R61 pad 1: U10_REXT -> +3V3
- R61 pad 2: GND -> BAY2_LED_A
- R62 pad 1: U10_VCCO -> +3V3
- R62 pad 2: U10_RST -> BAY3_LED_A
- R63 pad 1: U10_VCCO -> +3V3
- R63 pad 2: BAY1_LED_A -> BAY4_LED_A
- R64 pad 1: U10_XI -> +3V3
- R64 pad 2: GND -> BAY5_LED_A
- R65 pad 1: U10_XO -> +3V3
- R65 pad 2: GND -> BAY6_LED_A
- R66 pad 1: U10_VDD_CORE -> +3V3
- R66 pad 2: GND -> BAY7_LED_A
- R67 pad 1: U10_VDD_CORE -> +3V3
- R67 pad 2: GND -> BAY8_LED_A
- SW1 pad 1: GND -> DIP1
- SW1 pad 2: +3V3 -> DIP2
- SW1 pad 3: I2C1_SCL -> DIP3
- SW1 pad 4: I2C1_SDA -> DIP4
- SW3 pad 1: +12V -> M2_DOOR
- SW3 pad 2: Q20_GATE -> GND
- U1 pad 1: BAY3_USB2_DP -> BAY1_USB2_DP
- U1 pad 10: U2_DN2_TXDP -> U1_DN2_TXDP
- U1 pad 11: U2_DN2_TXDM -> U1_DN2_TXDM
- U1 pad 13: BAY4_USB3_TX_P -> BAY2_USB3_TX_P
- U1 pad 14: BAY4_USB3_TX_N -> BAY2_USB3_TX_N
- U1 pad 17: U2_PRT_DIS_P3 -> BAY3_USB2_DP
- U1 pad 18: U2_PRT_DIS_M3 -> BAY3_USB2_DM
- U1 pad 19: (no net) -> U1_DN3_TXDP
- U1 pad 2: BAY3_USB2_DM -> BAY1_USB2_DM
- U1 pad 20: (no net) -> U1_DN3_TXDM
- U1 pad 22: (no net) -> BAY3_USB3_TX_P
- U1 pad 23: (no net) -> BAY3_USB3_TX_N
- U1 pad 24: U2_PRT_DIS_P4 -> BAY4_USB2_DP
- U1 pad 25: U2_PRT_DIS_M4 -> BAY4_USB2_DM
- U1 pad 26: (no net) -> U1_DN4_TXDP
- U1 pad 27: (no net) -> U1_DN4_TXDM
- U1 pad 29: (no net) -> BAY4_USB3_TX_P
- U1 pad 3: U2_DN1_TXDP -> U1_DN1_TXDP
- U1 pad 30: (no net) -> BAY4_USB3_TX_N
- U1 pad 37: U2_VBUS_DET -> U1_VBUS_DET
- U1 pad 4: U2_DN1_TXDM -> U1_DN1_TXDM
- U1 pad 41: U2_CFG_NON_REM -> U1_CFG_NON_REM
- U1 pad 42: U2_RESET_N -> U1_RESET_N
- U1 pad 45: USB3_1_DP -> USB3_0_DP
- U1 pad 46: USB3_1_DM -> USB3_0_DM
- U1 pad 47: U2_UP_TXDP -> U1_UP_TXDP
- U1 pad 48: U2_UP_TXDM -> U1_UP_TXDM
- U1 pad 50: USB3_1_TX_P -> USB3_0_TX_P
- U1 pad 51: USB3_1_TX_N -> USB3_0_TX_N
- U1 pad 53: U2_XTALO -> U1_XTALO
- U1 pad 54: U2_XTALI -> U1_XTALI
- U1 pad 56: U2_RBIAS -> U1_RBIAS
- U1 pad 6: BAY3_USB3_TX_P -> BAY1_USB3_TX_P
- U1 pad 7: BAY3_USB3_TX_N -> BAY1_USB3_TX_N
- U1 pad 8: BAY4_USB2_DP -> BAY2_USB2_DP
- U1 pad 9: BAY4_USB2_DM -> BAY2_USB2_DM
- U2 pad 1: 5V_SYS -> BAY5_USB2_DP
- U2 pad 10: 5V_SYS -> U2_DN2_TXDP
- U2 pad 11: 5V_SYS -> U2_DN2_TXDM
- U2 pad 12: U10_VCCO -> +1V2
- U2 pad 13: U10_VDD_CORE -> BAY6_USB3_TX_P
- U2 pad 14: U10_VCCO -> BAY6_USB3_TX_N
- U2 pad 15: BAY1_USB2_DP -> +1V2
- U2 pad 16: BAY1_USB2_DM -> +3V3
- U2 pad 17: U10_REXT -> BAY7_USB2_DP
- U2 pad 18: U10_VCCO -> BAY7_USB2_DM
- U2 pad 19: U10_UTXN -> U2_DN3_TXDP
- U2 pad 2: (no net) -> BAY5_USB2_DM
- U2 pad 20: U10_UTXP -> U2_DN3_TXDM
- U2 pad 21: GND -> +1V2
- U2 pad 22: BAY1_USB3_RX_N -> BAY7_USB3_TX_P
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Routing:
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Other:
- board size 150 x 112 mm -> 150 x 122 mm
- board text added: "brain-drain brain v4 150x122 rear edge = top"
- board text removed: "brain-drain carrier v3 150x112 rear edge = top"
